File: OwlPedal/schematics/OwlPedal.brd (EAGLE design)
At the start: 103.1 x 79.5 mm, 87 parts, among them IC3 MC7805CDTG, IC6 TS974, J1 NEUTRIK_NMJ6HCD2, J2 NEUTRIK_NMJ6HCD2, J3 NEUTRIK_NMJ6HCD2, J4 NEUTRIK_NMJ6HCD2, J5 NEUTRIK_NMJ6HCD2, J6 NEUTRIK_NMJ6HCD2, J7 POWER_JACK, T1 BC846, T2 2N7002P

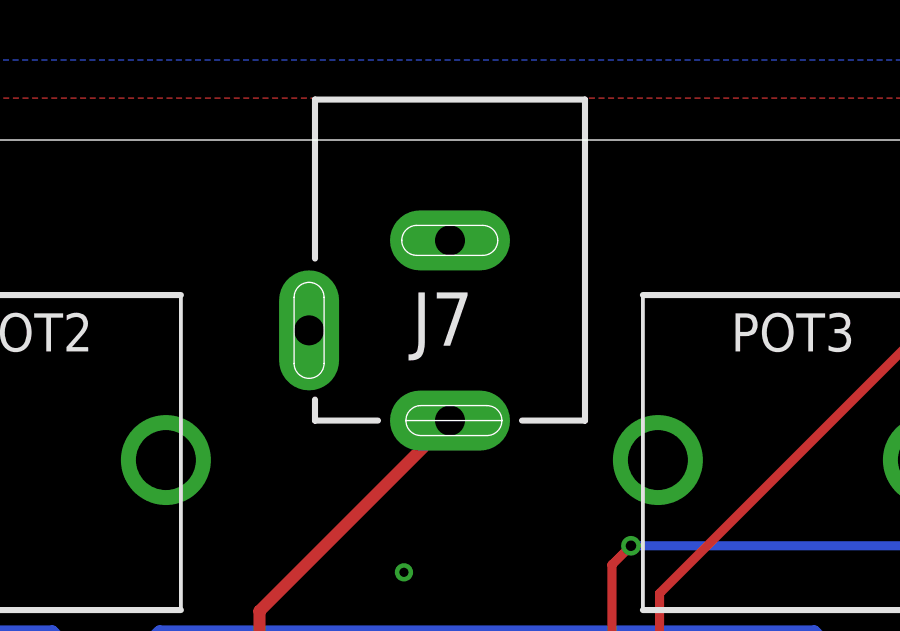
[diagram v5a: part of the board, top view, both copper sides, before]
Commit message: changed 22u cap to 1u film
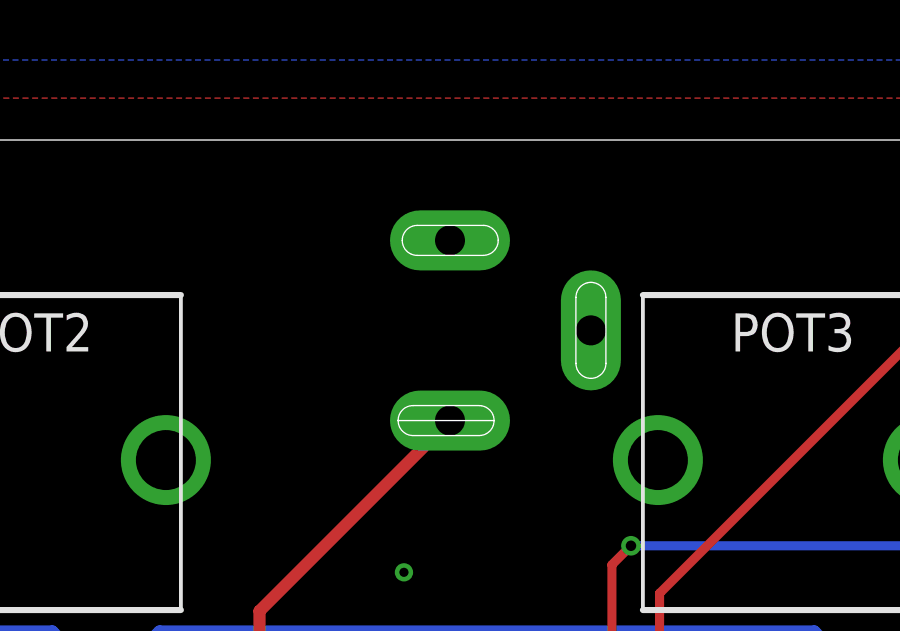
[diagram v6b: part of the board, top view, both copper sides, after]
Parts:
- C16, C19: value 1u -> 1u Film
- C21, C5: value 22u -> 1u Film
- IC6: value TS974 -> TS924
- flipped J7 to the bottom
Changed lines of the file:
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@@
 <?xml version="1.0" encoding="utf-8"?>
 <!DOCTYPE eagle SYSTEM "eagle.dtd">
-<eagle version="9.4.0">
+<eagle version="9.6.1">
 <drawing>
 <settings>
-<setting alwaysvectorfont="yes"/>
+<setting alwaysvectorfont="no"/>
 <setting keepoldvectorfont="yes"/>
 <setting verticaltext="up"/>
@@
 <attribute name="VALUE" x="25.435" y="59.8" size="1.016" layer="27" rot="R270"/>
 </element>
-<element name="IC6" library="linear" package="SO14" value="TS974" x="65.405" y="47.625" smashed="yes" rot="R180">
+<element name="IC6" library="linear" package="SO14" value="TS924" x="65.405" y="47.625" smashed="yes" rot="R180">
 <attribute name="NAME" x="64.262" y="48.26" size="0.762" layer="25" font="vector" rot="R270"/>
 <attribute name="VALUE" x="59.563" y="49.53" size="1.27" layer="27" rot="R270"/>
 </element>
-<element name="C16" library="Rebel" package="C1210" value="1u" x="41.91" y="27.6225" smashed="yes" rot="R180">
+<element name="C16" library="Rebel" package="C1210" value="1u Film" x="41.91" y="27.6225" smashed="yes" rot="R180">
 <attribute name="NAME" x="38.66" y="28.5875" size="0.762" layer="25" font="vector" rot="R270"/>
 <attribute name="VALUE" x="41.225" y="30.8575" size="1.27" layer="27" rot="R270"/>
@@
 <attribute name="VALUE" x="70.739" y="57.912" size="1.27" layer="27" rot="R180"/>
 </element>
-<element name="C19" library="Rebel" package="C1210" value="1u" x="52.07" y="30.48" smashed="yes">
+<element name="C19" library="Rebel" package="C1210" value="1u Film" x="52.07" y="30.48" smashed="yes">
 <attribute name="NAME" x="48.835" y="31.405" size="0.762" layer="25" font="vector" rot="R270"/>
 <attribute name="VALUE" x="49.795" y="26.745" size="1.27" layer="27"/>
@@
 <attribute name="VALUE" x="61.5315" y="54.737" size="1.27" layer="27" rot="R180"/>
 </element>
-<element name="C21" library="Rebel" package="C1210" value="22u" x="55.88" y="53.34" smashed="yes" rot="R90">
+<element name="C21" library="Rebel" package="C1210" value="1u Film" x="55.88" y="53.34" smashed="yes" rot="R90">
 <attribute name="NAME" x="54.356" y="52.705" size="0.762" layer="25" font="vector" rot="R90" align="bottom-center"/>
 </element>
@@
 <attribute name="NAME" x="12.7" y="37.338" size="1.016" layer="25" font="vector" rot="R180" align="bottom-center"/>
 </element>
-<element name="C5" library="Rebel" package="C1210" value="22u" x="56.8325" y="36.83" smashed="yes" rot="R270">
+<element name="C5" library="Rebel" package="C1210" value="1u Film" x="56.8325" y="36.83" smashed="yes" rot="R270">
 <attribute name="NAME" x="56.8325" y="33.5915" size="0.762" layer="25" font="vector" align="bottom-center"/>
 </element>
@@
 <attribute name="NAME" x="13.335" y="13.462" size="1.016" layer="25" font="vector" align="bottom-center"/>
 </element>
-<element name="J7" library="Rebel" package="DC_JACK_SLOT" value="POWER_JACK" x="52.07" y="81.915" smashed="yes" rot="R180">
-<attribute name="NAME" x="50.8" y="73.66" size="1.778" layer="25" font="vector"/>
-<attribute name="VALUE" x="59.69" y="78.6465" size="0.4064" layer="27"/>
+<element name="J7" library="Rebel" package="DC_JACK_SLOT" value="POWER_JACK" x="52.07" y="81.915" smashed="yes" rot="MR180">
+<attribute name="NAME" x="53.34" y="73.66" size="1.778" layer="26" font="vector" rot="MR0"/>
+<attribute name="VALUE" x="44.45" y="78.6465" size="0.4064" layer="28" rot="MR0"/>
 </element>
 <element name="JP6" library="SparkFun" package="1X02" value="" x="63.1825" y="21.2725" smashed="yes">

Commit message: OwlPedal2 Rev02
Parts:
- removed IC3: MC7805CDTG, James:DPACK
- removed JP7: (no value), SparkFun:1X02
- removed SWD1: (no value), SparkFun:1X06
- added IC1: 7805TV, linear:TO220V
- added R25, R27: 150R, Rebel:0603
- added SWD2: (no value), SparkFun:1X06
- moved R21 43.3 mm to (56.0, 55.4), turned to 0 degrees
- moved R22 41.1 mm to (53.7, 32.6), turned to 0 degrees
- moved C21 6.60 mm to (59.2, 47.6)
- moved R38 4.45 mm to (56.0, 52.7)
- moved SWD 2.54 mm to (20.0, 59.4)
- moved C16 1.91 mm to (43.8, 27.6)
- moved R26 1.91 mm to (43.8, 25.1)
- moved C19 1.27 mm to (52.1, 29.2)
- moved R13 1.27 mm to (52.1, 26.7)
- moved R7 0.89 mm to (60.6, 58.7)
- moved R8 0.89 mm to (69.8, 58.7)
- moved C18 0.76 mm to (69.8, 56.6)
- moved C4 0.76 mm to (60.6, 56.6)
- moved R10 0.38 mm to (69.8, 54.7)
- moved R11 0.38 mm to (60.6, 54.7)
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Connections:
- removed net A3_USART_TX: LGP1-5.3, R24.2
- removed net A4_USART_RX: LGP1-5.4, R23.2
- removed net A6: JP7.2, R2.2
- removed net A7: JP7.1, R1.2
- new net A3: LGP1-5.3, R2.2
- new net A4: LGP1-5.4, R1.2
- new net N$1: J5.RN, J5.TN, R25.2
- new net N$4: J6.RN, J6.TN, R27.2
- net +3V3: now also R25.1, R27.1; no longer J5.RN, J5.TN
- net +5V: now also IC1.3; no longer IC3.3
- net A1: now also R24.2
- net A2: now also R23.2
- net FX_IN_L: now also C16.2, R26.1
- net FX_IN_R: now also C19.2, R13.1
- net FX_OUT_L: now also R21.1, R38.2
- net FX_OUT_R: now also R15.2, R22.1
- net GND: now also IC1.2; no longer IC3.4
- net IN_L: no longer C16.2, R26.1
- net IN_R: no longer C19.2, R13.1
- net N$3: now also SWD2.1; no longer SWD1.1
- net N$5: now also SWD2.2; no longer SWD1.2
- net N$51: now also IC1.1; no longer IC3.1
- net N$6: now also SWD2.3; no longer SWD1.3
- net N$7: now also SWD2.4; no longer SWD1.4
- net N$8: now also SWD2.5; no longer SWD1.5
- net N$9: now also SWD2.6; no longer SWD1.6
- net OUT_L: no longer R21.1, R38.2
- net OUT_R: no longer R15.2, R22.1
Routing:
- net +3V3: track 164.3 -> 223.1 mm
- net A4_USART_RX: track 51.8 -> 0.00 mm, vias 1 -> 0
- net A3_USART_TX: track 49.8 -> 0.00 mm, vias 1 -> 0
- net A2: track 0.00 -> 46.8 mm, vias 0 -> 1
- net A1: track 0.00 -> 43.7 mm, vias 0 -> 1
- net A4: track 0.00 -> 40.5 mm, vias 0 -> 2
- net A3: track 0.00 -> 38.5 mm, vias 0 -> 1
- net FX_OUT_L: track 0.00 -> 37.1 mm
- net A7: track 29.4 -> 0.00 mm, vias 2 -> 0
- net A6: track 26.9 -> 0.00 mm
- net FX_OUT_R: track 0.00 -> 20.4 mm
- net N$4: track 0.00 -> 17.1 mm
- net N$1: track 0.00 -> 10.3 mm
- net FX_IN_R: track 0.00 -> 9.20 mm
- net OUT_L: track 85.4 -> 77.6 mm
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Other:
- board text added: "GND"
- board text added: "OWL MkII Rev02"
- board text added: "VBUS"
- board text removed: "OWL MkII Rev01"
